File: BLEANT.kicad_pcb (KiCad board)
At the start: 2 copper layers, 75.8 x 76.2 mm, 27 parts, among them J1 Conn_01x04_Male, J2 SC_19-20, U1 nRF51x22-QFxx, U2 LM50BIM3, X1 16MHz, X2 32.768kHz

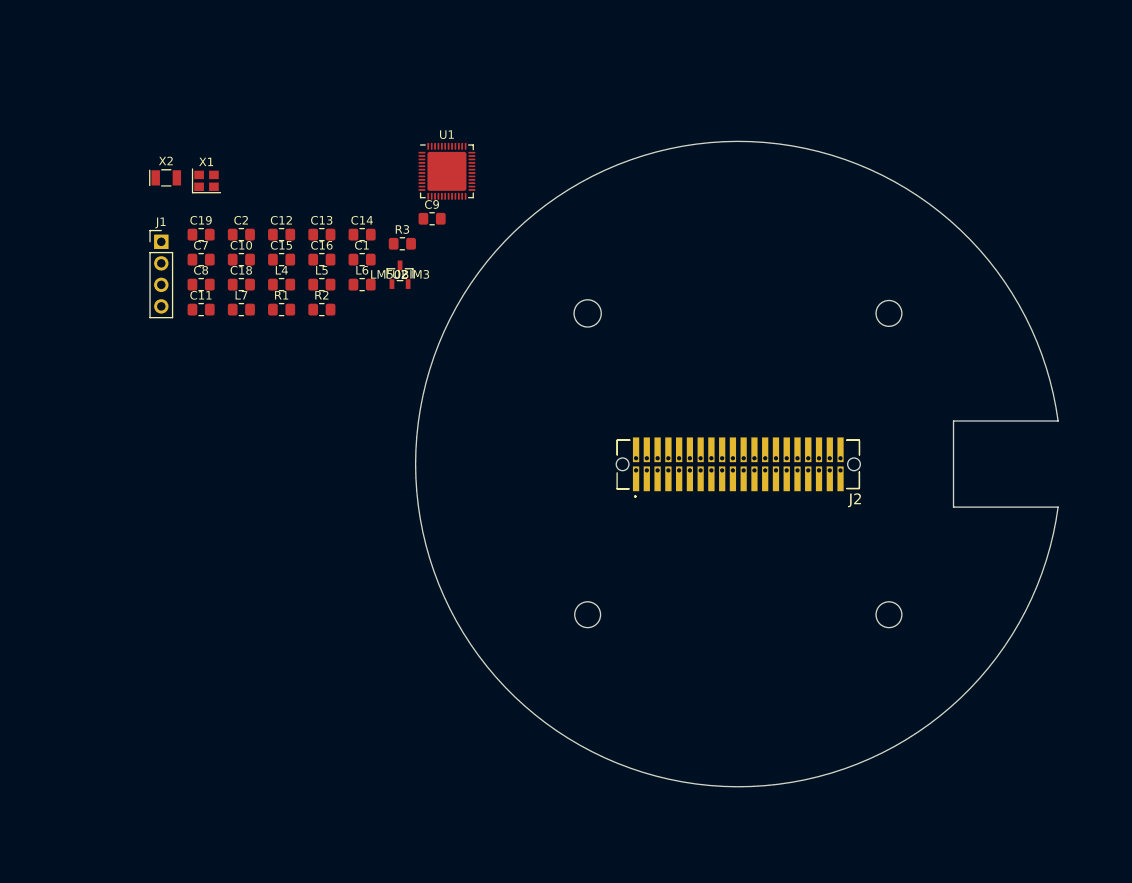
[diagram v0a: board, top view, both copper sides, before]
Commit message: added matching network. ruined half the other routing
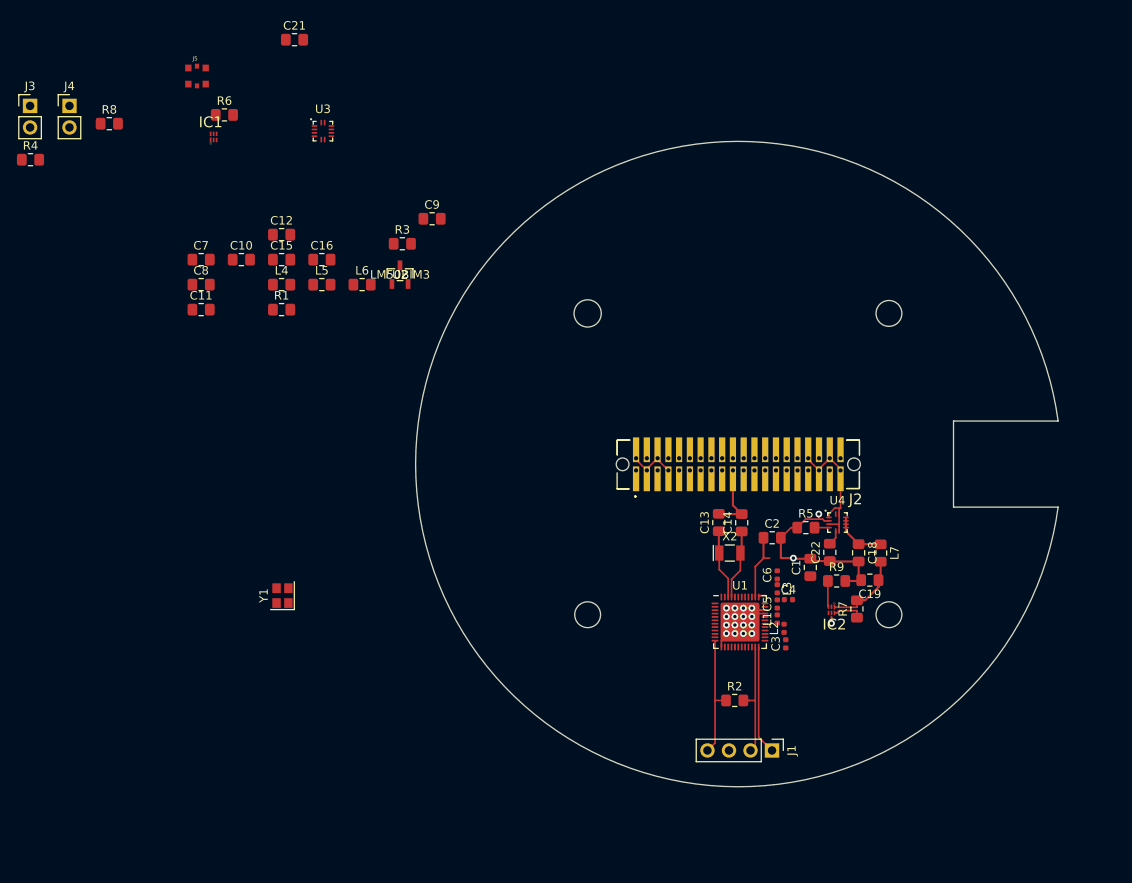
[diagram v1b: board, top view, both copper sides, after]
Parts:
- removed X1: 16MHz, Crystal:Crystal_SMD_2520-4Pin_2.5x2.0mm
- added C21: 0.54uF, Capacitor_SMD:C_0805_2012Metric_Pad1.15x1.40mm_HandSolder, F.Cu at (100.0, 76.9)
- added C22: 0.9uF, Capacitor_SMD:C_0805_2012Metric_Pad1.15x1.40mm_HandSolder, F.Cu at (163.2, 137.4)
- added C3: 2.2nF, Capacitor_SMD:C_0402_1005Metric, F.Cu at (158.0, 148.2)
- added C4: 1pF, Capacitor_SMD:C_0402_1005Metric, F.Cu at (158.3, 143.0)
- added C5: 2.2pF, Capacitor_SMD:C_0402_1005Metric, F.Cu at (157.0, 143.5)
- added C6: 1.5pF, Capacitor_SMD:C_0402_1005Metric, F.Cu at (157.0, 140.1)
- added G***: LOGO, Layer 1:L1, F.Cu at (152.3, 144.0)
- added IC1: FAN4010IL6X_F113, FAN4010:6-LEAD_MICROPAK, F.Cu at (90.5, 88.4)
- added IC2: FAN4010IL6X_F113, FAN4010:6-LEAD_MICROPAK, F.Cu at (163.4, 144.2)
- added J3: Conn_01x02, Connector_PinHeader_2.54mm:PinHeader_1x02_P2.54mm_Vertical, F.Cu at (68.8, 84.7)
- added J4: Conn_01x02, Connector_PinHeader_2.54mm:PinHeader_1x02_P2.54mm_Vertical, F.Cu at (73.5, 84.7)
- added J5: MM8130-2600RA2, MM8130:MURATA_MM8130-2600RA2, F.Cu at (88.5, 81.2)
- added L1: 4.7nH, Inductor_SMD:L_0402_1005Metric, F.Cu at (157.0, 145.3)
- added L2: 10nH, Inductor_SMD:L_0402_1005Metric, F.Cu at (157.8, 146.4)
- added L3: 3.3nH, Inductor_SMD:L_0402_1005Metric, F.Cu at (157.0, 141.7)
- added R4: 820k, Resistor_SMD:R_0805_2012Metric_Pad1.15x1.40mm_HandSolder, F.Cu at (68.9, 91.1)
- added R5: 820k, Resistor_SMD:R_0805_2012Metric_Pad1.15x1.40mm_HandSolder, F.Cu at (160.4, 134.5)
- added R6: 1, Resistor_SMD:R_0805_2012Metric_Pad1.15x1.40mm_HandSolder, F.Cu at (91.7, 85.8)
- added R7: R, Resistor_SMD:R_0805_2012Metric_Pad1.15x1.40mm_HandSolder, F.Cu at (166.4, 144.1)
- added R8: 3k, Resistor_SMD:R_0805_2012Metric_Pad1.15x1.40mm_HandSolder, F.Cu at (78.2, 86.8)
- added R9: R, Resistor_SMD:R_0805_2012Metric_Pad1.15x1.40mm_HandSolder, F.Cu at (164.0, 140.8)
- added U3: MP5077GG-Z, MASA_Library:MP5077GG-Z, F.Cu at (103.4, 87.7)
- added U4: MP5077GG-Z, MASA_Library:MP5077GG-Z, F.Cu at (164.1, 133.9)
- added Y1: 16MHz, Crystal:Crystal_SMD_2520-4Pin_2.5x2.0mm, F.Cu at (98.6, 142.5)
- moved J1 93.8 mm to (156.4, 160.8), turned to 270 degrees
- moved C19 88.8 mm to (167.9, 140.7), turned to 180 degrees
- moved L7 80.7 mm to (169.2, 137.5), turned to 270 degrees
- moved X2 79.9 mm to (151.4, 137.5)
- moved C18 79.4 mm to (166.6, 137.5), turned to 270 degrees
- moved C2 72.1 mm to (156.4, 135.7)
- moved R2 67.1 mm to (152.0, 154.9)
- moved C1 64.2 mm to (160.9, 139.2), turned to 90 degrees
- moved U1 63.5 mm to (152.6, 145.6)
- moved C13 57.9 mm to (150.1, 133.9), turned to 90 degrees
- moved C14 56.2 mm to (152.8, 133.9), turned to 90 degrees
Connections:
- C16 pad 1: +3V3 -> Net-(C16-Pad1)
- C19 pad 1: +5V -> Net-(C19-Pad1)
- J1 pad 1: Net-(J1-Pad1) -> SWDCLK
- J1 pad 2: Net-(J1-Pad2) -> SWDIO
- L6 pad 2: +3V3 -> Net-(C16-Pad1)
- L7 pad 2: +5V -> Net-(C19-Pad1)
- R2 pad 2: Net-(J1-Pad1) -> SWDIO
- U1 pad 23: Net-(J1-Pad1) -> SWDIO
- U1 pad 24: Net-(J1-Pad2) -> SWDCLK
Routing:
- net GND: track 0.00 -> 43.2 mm, vias 0 -> 19
- net 5V0: track 0.00 -> 16.4 mm
- net +3V3: track 0.00 -> 14.6 mm
- net SWDIO: track 0.00 -> 13.8 mm
- net SWDCLK: track 0.00 -> 12.9 mm
- net Net-(C19-Pad1): track 0.00 -> 9.75 mm
- net XL2: track 0.00 -> 8.24 mm
- net XL1: track 0.00 -> 8.23 mm
- net Net-(C2-Pad1): track 0.00 -> 8.12 mm
- net Net-(C18-Pad1): track 0.00 -> 6.56 mm
- net 3V3: track 0.00 -> 5.87 mm
- net +5V: track 0.00 -> 3.53 mm
- net 5V0Sense: track 0.00 -> 3.05 mm
- net Net-(C22-Pad2): track 0.00 -> 1.79 mm
- net Net-(R5-Pad2): track 0.00 -> 1.70 mm
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- added copper zone on In1.Cu, net GND
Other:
- copper layers 2 -> 4

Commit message: Placed all components. Need to add GPIO connections
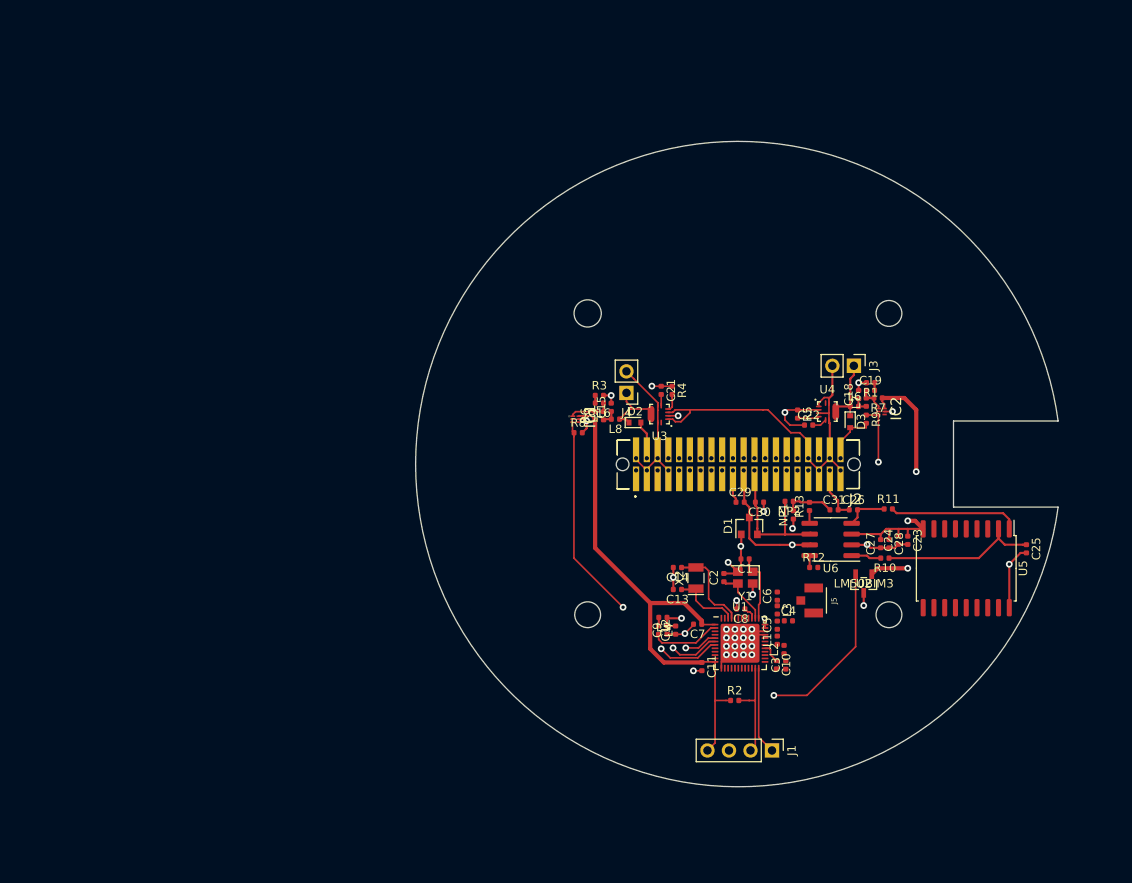
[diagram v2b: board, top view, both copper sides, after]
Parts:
- removed G***: LOGO, Layer 1:L1
- added C23: 100nf, Capacitor_SMD:C_0402_1005Metric, F.Cu at (172.4, 136.0)
- added C24: 1nf, Capacitor_SMD:C_0402_1005Metric, F.Cu at (171.3, 136.0)
- added C25: 100pf, Capacitor_SMD:C_0402_1005Metric, F.Cu at (186.4, 137.0)
- added C26: 100pf, Capacitor_SMD:C_0402_1005Metric, F.Cu at (166.0, 132.4)
- added C27: 1nf, Capacitor_SMD:C_0402_1005Metric, F.Cu at (169.2, 136.4)
- added C28: 100nf, Capacitor_SMD:C_0402_1005Metric, F.Cu at (170.2, 136.4)
- added C29: 100pf, Capacitor_SMD:C_0402_1005Metric, F.Cu at (152.6, 131.5)
- added C30: 100pf, Capacitor_SMD:C_0402_1005Metric, F.Cu at (154.9, 131.5)
- added C31: 1nf, Capacitor_SMD:C_0402_1005Metric, F.Cu at (163.7, 132.4)
- added D1: D5V0L2B3W-7, Package_TO_SOT_SMD:SOT-23, F.Cu at (153.7, 134.3)
- added D2: D_TVS, Diode_SMD:D_SOD-523, F.Cu at (140.2, 122.1)
- added D3: D_TVS, Diode_SMD:D_SOD-523, F.Cu at (165.6, 122.0)
- added L8: 2.2uH, Inductor_SMD:L_0402_1005Metric, F.Cu at (137.9, 121.7)
- added L9: 1uH, Inductor_SMD:L_0402_1005Metric, F.Cu at (136.5, 121.3)
- added NP1: 120, Resistor_SMD:R_0402_1005Metric, F.Cu at (158.9, 133.0)
- added NP2: 120, Resistor_SMD:R_0402_1005Metric, F.Cu at (158.4, 131.4)
- added R10: 0, Resistor_SMD:R_0402_1005Metric, F.Cu at (169.7, 138.1)
- added R11: 0, Resistor_SMD:R_0402_1005Metric, F.Cu at (170.1, 132.3)
- added R12: 10k, Resistor_SMD:R_0402_1005Metric, F.Cu at (161.3, 139.2)
- added R13: 0, Resistor_SMD:R_0402_1005Metric, F.Cu at (160.8, 132.0)
- added U5: MCP2515-xSO, Package_SO:SOIC-18W_7.5x11.6mm_P1.27mm, F.Cu at (179.3, 139.3)
- added U6: SN65HVD1050D, Package_SO:SOIC-8_3.9x4.9mm_P1.27mm, F.Cu at (163.3, 135.9)
- C1, C10, C11, C12, C13, C14, C2, C21, C22, C7, C8, C9: footprint Capacitor_SMD:C_0805_2012Metric_Pad1.15x1.40mm_HandSolder -> Capacitor_SMD:C_0402_1005Metric
- C15, C18: value 1nF -> 10nF; footprint Capacitor_SMD:C_0805_2012Metric_Pad1.15x1.40mm_HandSolder -> Capacitor_SMD:C_0402_1005Metric
- C16, C19: value 18uF -> 3.3uF; footprint Capacitor_SMD:C_0805_2012Metric_Pad1.15x1.40mm_HandSolder -> Capacitor_SMD:C_0402_1005Metric
- J5: value MM8130-2600RA2 -> 1909763-1; footprint MM8130:MURATA_MM8130-2600RA2 -> U:TE_1909763-1
- L4, L5: footprint Inductor_SMD:L_0805_2012Metric_Pad1.15x1.40mm_HandSolder -> Inductor_SMD:L_0402_1005Metric
- L6: value 9.1uH -> 2.2uH; footprint Inductor_SMD:L_0805_2012Metric_Pad1.15x1.40mm_HandSolder -> Inductor_SMD:L_0402_1005Metric
- L7: value 9.1uH -> 1uH; footprint Inductor_SMD:L_0805_2012Metric_Pad1.15x1.40mm_HandSolder -> Inductor_SMD:L_0402_1005Metric
- R1, R3: value 700m -> 15; footprint Resistor_SMD:R_0805_2012Metric_Pad1.15x1.40mm_HandSolder -> Resistor_SMD:R_0402_1005Metric
- R2, R4, R5, R6, R7, R8, R9: footprint Resistor_SMD:R_0805_2012Metric_Pad1.15x1.40mm_HandSolder -> Resistor_SMD:R_0402_1005Metric
- moved J3 101.9 mm to (166.0, 115.4), turned to 270 degrees
- moved J5 95.5 mm to (161.3, 143.1), turned to 270 degrees
- moved R4 80.5 mm to (144.6, 118.3), turned to 270 degrees
- moved C10 79.2 mm to (156.9, 150.7), turned to 270 degrees
- moved C8 74.3 mm to (152.7, 144.1), turned to 180 degrees
- moved J4 73.9 mm to (139.2, 118.6), turned to 180 degrees
- moved C7 72.7 mm to (147.6, 145.9), turned to 180 degrees
- moved C11 72.6 mm to (148.1, 150.9), turned to 270 degrees
- moved R1 70.0 mm to (168.0, 117.4), turned to 180 degrees
- moved R8 66.3 mm to (133.5, 123.3)
- moved C12 65.9 mm to (145.0, 146.6), turned to 90 degrees
- moved U2 65.8 mm to (167.2, 141.1), turned to 180 degrees
- moved L4 60.4 mm to (143.0, 146.6), turned to 270 degrees
- moved C21 59.9 mm to (143.3, 118.3), turned to 270 degrees
- moved L6 59.9 mm to (166.1, 120.2)
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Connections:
- C16 pad 2: GND -> Net-(C16-Pad2)
- C19 pad 2: GND -> Net-(C19-Pad2)
- J2 pad 21: Net-(J2-Pad21) -> CAN_H
- J2 pad 23: Net-(J2-Pad23) -> CAN_L
- J3 pad 1: Net-(C18-Pad1) -> Net-(D3-Pad1)
- J4 pad 1: Net-(C15-Pad1) -> Net-(D2-Pad1)
- L6 pad 1: Net-(C15-Pad1) -> Net-(D3-Pad1)
- L6 pad 2: Net-(C16-Pad1) -> Net-(C18-Pad1)
- R1 pad 1: GND -> Net-(C19-Pad2)
- R1 pad 2: Net-(C17-Pad2) -> GND
- R3 pad 1: GND -> Net-(C16-Pad2)
- R3 pad 2: Net-(C20-Pad2) -> GND
- U1 pad 5: Net-(U1-Pad5) -> Temperature
- U1 pad 6: Net-(U1-Pad6) -> 5V0Sense
- U1 pad 7: Net-(U1-Pad7) -> 3V3Sense
- U3 pad 10: Net-(C15-Pad1) -> Net-(D2-Pad1)
- U3 pad 7: Net-(C15-Pad1) -> Net-(D2-Pad1)
- U3 pad 8: Net-(C15-Pad1) -> Net-(D2-Pad1)
- U3 pad 9: Net-(C15-Pad1) -> Net-(D2-Pad1)
- U4 pad 10: Net-(C18-Pad1) -> Net-(D3-Pad1)
- U4 pad 7: Net-(C18-Pad1) -> Net-(D3-Pad1)
- U4 pad 8: Net-(C18-Pad1) -> Net-(D3-Pad1)
- U4 pad 9: Net-(C18-Pad1) -> Net-(D3-Pad1)
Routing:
- net 5V0Sense: track 3.05 -> 69.4 mm, vias 0 -> 2
- net +3V3: track 14.6 -> 61.8 mm
- net GND: track 43.2 -> 85.6 mm, vias 19 -> 34
- net Temperature: track 0.00 -> 41.6 mm, vias 0 -> 2
- net +5V: track 3.53 -> 44.2 mm, vias 0 -> 3
- net 3V3Sense: track 0.00 -> 39.5 mm, vias 0 -> 2
- net 5V0: track 16.4 -> 45.9 mm
- net CAN_H: track 0.00 -> 19.4 mm, vias 0 -> 2
- net Net-(C25-Pad1): track 0.00 -> 18.6 mm
- net CAN_L: track 0.00 -> 18.1 mm
- net Net-(R11-Pad2): track 0.00 -> 15.4 mm
- net Net-(C12-Pad2): track 0.00 -> 14.7 mm, vias 0 -> 2
- net 3V3: track 5.87 -> 17.7 mm
- net Net-(D3-Pad1): track 0.00 -> 9.00 mm
- net Net-(D2-Pad1): track 0.00 -> 8.94 mm
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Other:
- net class Default: clearance 0.2 -> 0.15
- rule trace_clearance: 0.2 -> 0.15

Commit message: Connected all IO lines
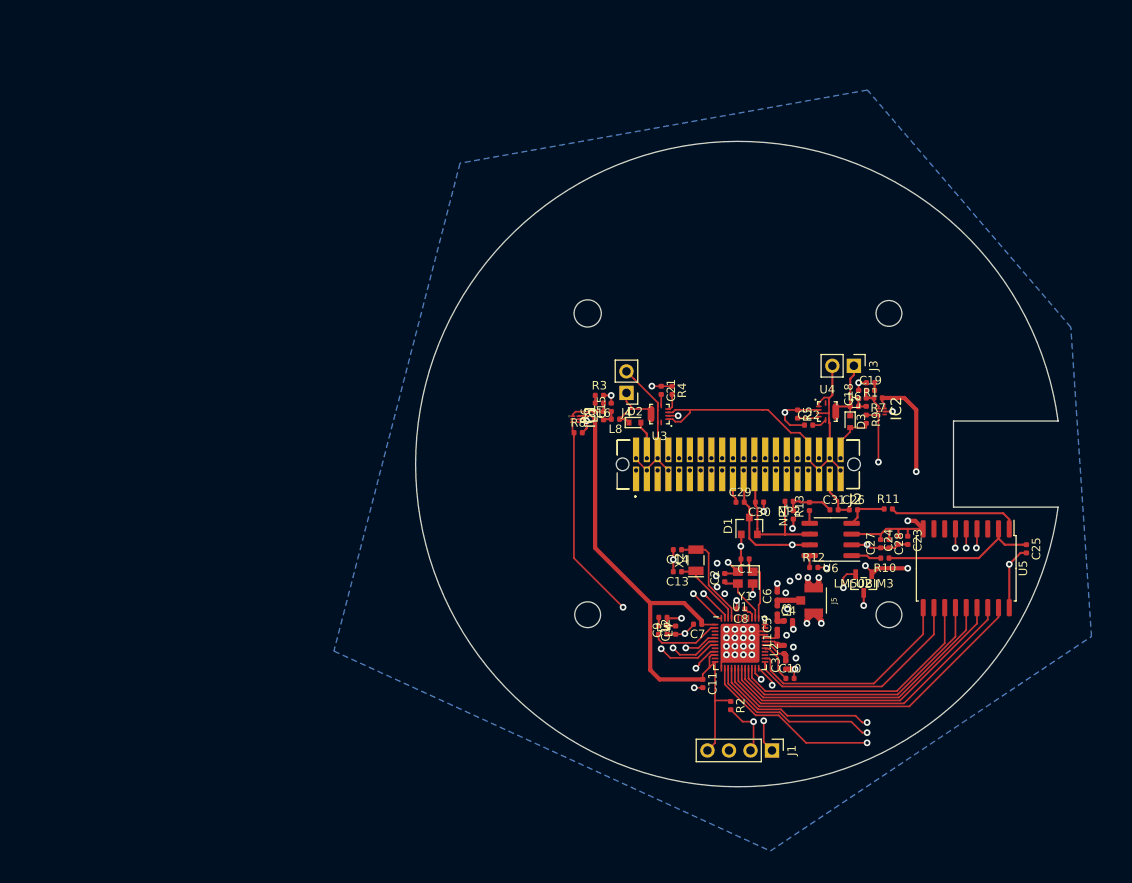
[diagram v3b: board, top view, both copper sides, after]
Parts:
- moved C10 2.27 mm to (158.5, 152.3), turned to 0 degrees
- moved C13 2.10 mm to (145.2, 139.7)
- moved C14 2.10 mm to (145.2, 137.1)
- moved X2 2.10 mm to (147.4, 138.3)
- moved C11 2.00 mm to (148.2, 152.9)
- moved R2 0.77 mm to (151.5, 155.5), turned to 270 degrees
- moved C2 0.10 mm to (150.8, 140.4)
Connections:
- J2 pad 29: Net-(J2-Pad29) -> UART_TX
- J2 pad 31: Net-(J2-Pad31) -> UART_RX
- U1 pad 10: Net-(U1-Pad10) -> +3V3
- U1 pad 14: Net-(U1-Pad14) -> TX0RTS
- U1 pad 15: Net-(U1-Pad15) -> TX1RTS
- U1 pad 16: Net-(U1-Pad16) -> TX2RTS
- U1 pad 17: Net-(U1-Pad17) -> CAN_RST
- U1 pad 18: Net-(U1-Pad18) -> CS
- U1 pad 19: Net-(U1-Pad19) -> MISO
- U1 pad 20: Net-(U1-Pad20) -> MOSI
- U1 pad 21: Net-(U1-Pad21) -> SCK
- U1 pad 22: Net-(U1-Pad22) -> CAN_INT
- U1 pad 25: Net-(U1-Pad25) -> RX0BF
- U1 pad 26: Net-(U1-Pad26) -> RX1BF
- U1 pad 47: Net-(U1-Pad47) -> UART_RX
- U1 pad 48: Net-(U1-Pad48) -> UART_TX
- U1 pad 5: Temperature -> +5V
- U1 pad 9: Net-(U1-Pad9) -> Temperature
- U5 pad 10: /CAN_Template/RX1BF -> RX1BF
- U5 pad 11: /CAN_Template/RX0BF -> RX0BF
- U5 pad 12: /CAN_Template/INT -> CAN_INT
- U5 pad 13: /CAN_Template/SCK -> SCK
- U5 pad 14: /CAN_Template/SI -> MOSI
- U5 pad 15: /CAN_Template/SO -> MISO
- U5 pad 16: /CAN_Template/CS -> CS
- U5 pad 17: /CAN_Template/RESET -> CAN_RST
- U5 pad 4: /CAN_Template/TX0RTS -> TX0RTS
- U5 pad 5: /CAN_Template/TX1RTS -> TX1RTS
- U5 pad 6: /CAN_Template/TX2RTS -> TX2RTS
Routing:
- net TX0RTS: track 0.00 -> 53.1 mm, vias 0 -> 2
- net +5V: track 44.2 -> 95.3 mm, vias 3 -> 5
- net TX1RTS: track 0.00 -> 50.8 mm, vias 0 -> 2
- net TX2RTS: track 0.00 -> 48.5 mm, vias 0 -> 2
- net CAN_RST: track 0.00 -> 39.4 mm
- net CS: track 0.00 -> 37.5 mm
- net MISO: track 0.00 -> 35.8 mm
- net MOSI: track 0.00 -> 34.2 mm
- net SCK: track 0.00 -> 32.7 mm
- net CAN_INT: track 0.00 -> 31.1 mm
- net RX0BF: track 0.00 -> 27.4 mm
- net RX1BF: track 0.00 -> 26.2 mm
- net UART_TX: track 0.00 -> 25.0 mm, vias 0 -> 1
- net UART_RX: track 0.00 -> 24.8 mm, vias 0 -> 1
- net GND: track 85.6 -> 97.0 mm, vias 34 -> 53
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- added copper zone on B.Cu, net GND

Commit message: Added BOM
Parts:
- C21: value 0.54uF -> 0.56uF
- C22: value 0.9uF -> 1uF
- L4: footprint Inductor_SMD:L_0402_1005Metric -> Inductor_SMD:L_0603_1608Metric
- R7: value R -> 1
- R9: value R -> 3k
- moved L4 0.21 mm to (143.0, 146.8)
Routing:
- net Net-(L4-Pad2): track 8.16 -> 7.55 mm
